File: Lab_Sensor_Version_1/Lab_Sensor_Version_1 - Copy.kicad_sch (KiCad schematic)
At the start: 28 parts, among them U1 ESP32-POE, U2 AM2302, U3 SSD1306, U4 INMP441

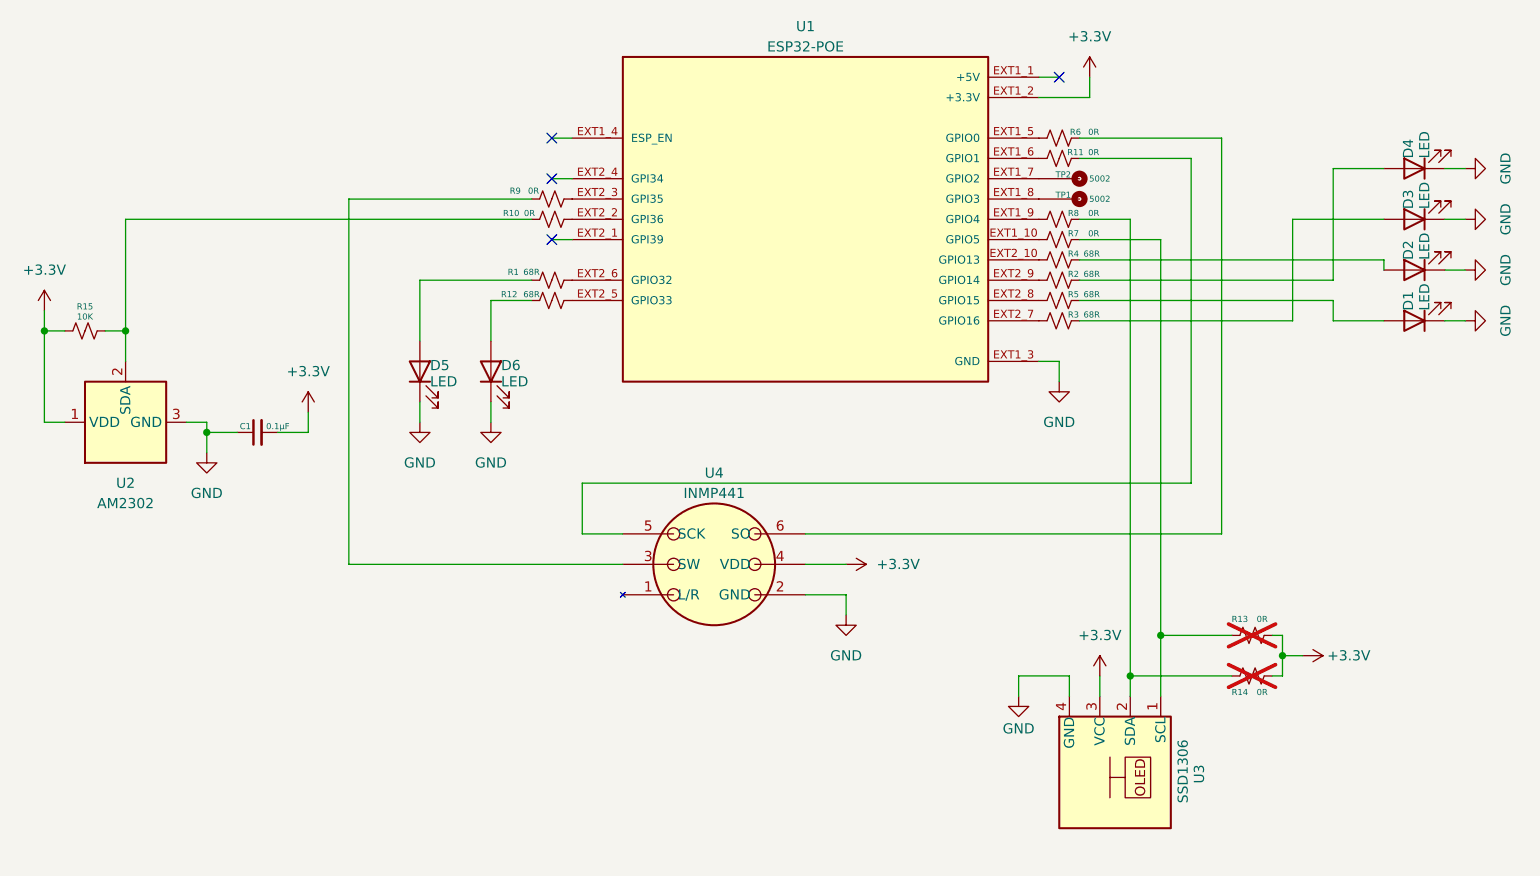
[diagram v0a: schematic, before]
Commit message: Signals on PCB connected
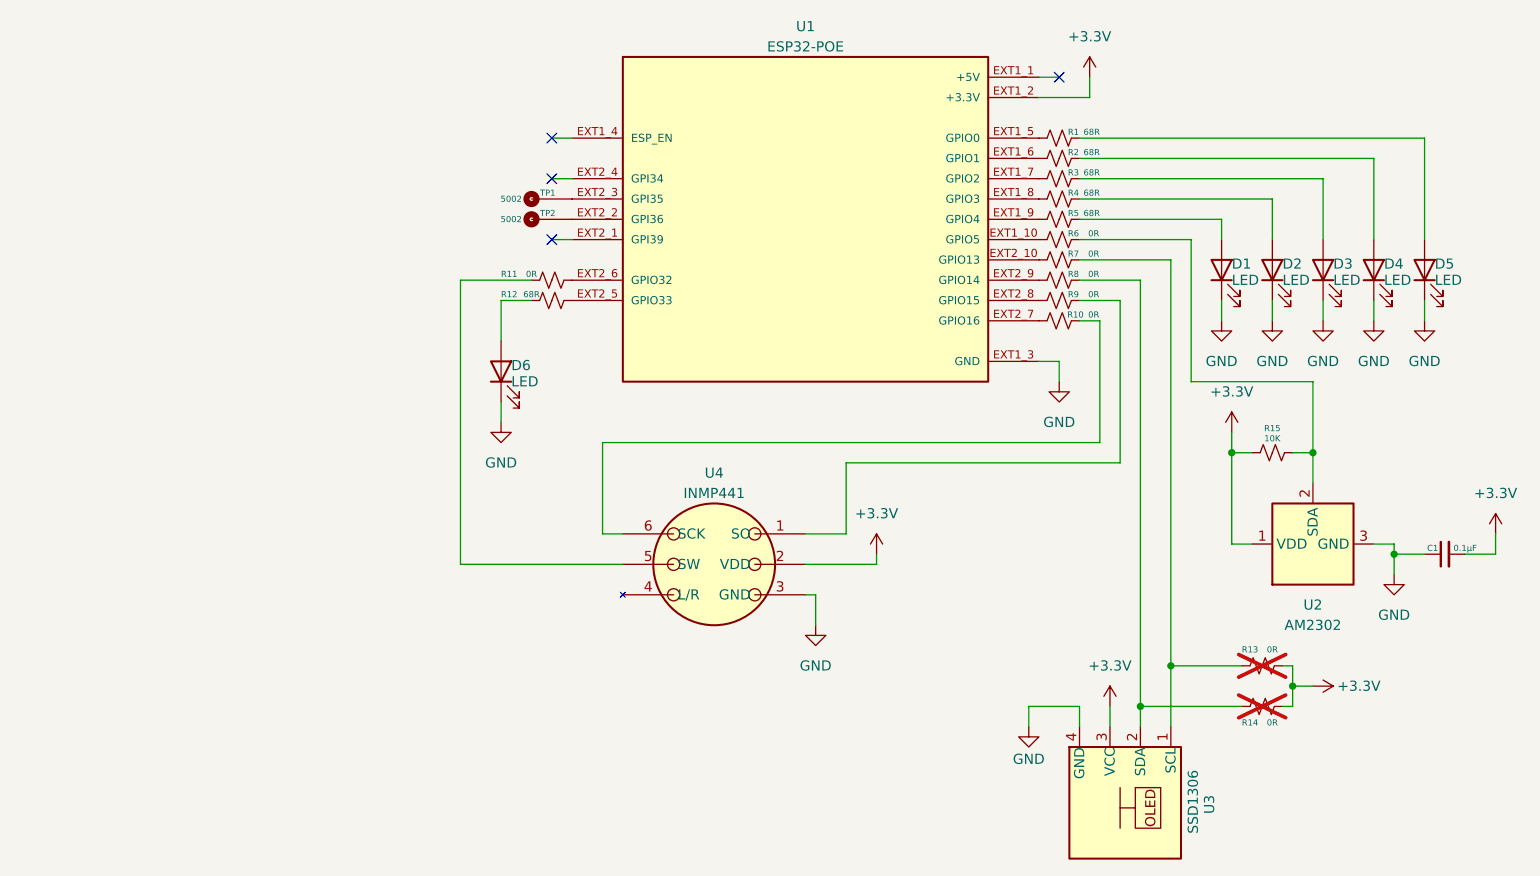
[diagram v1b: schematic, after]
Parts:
- renumbered R6 to R10, R10 to R6
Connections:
- net +3.3V: now also U4.2 (VDD); no longer U4.4 (VDD)
- net GND: now also U4.3 (GND); no longer U4.2 (GND)
- net at R3.2: now also U1.EXT1_7 (GPIO2); no longer U1.EXT2_7 (GPIO16)
- net at R9.1: now also U4.1 (SO); no longer U1.EXT2_3 (GPI35)
- net at R9.2: now also U1.EXT2_8 (GPIO15); no longer U4.3 (SW)
- net at R6.1: now also R15.1, U2.2 (SDA); no longer U1.EXT2_2 (GPI36)
- net at U1.EXT1_10 (GPIO5): now also R6.2; no longer R7.2
- net at TP1.TP: now also U1.EXT2_3 (GPI35); no longer U1.EXT1_8 (GPIO3)
- net at R8.2: now also U1.EXT2_9 (GPIO14); no longer U1.EXT1_9 (GPIO4)
- net at R10.2: now also U1.EXT2_7 (GPIO16); no longer U1.EXT1_5 (GPIO0)
- net at U1.EXT1_6 (GPIO1): now also R2.2; no longer R11.2
- net at TP2.TP: now also U1.EXT2_2 (GPI36); no longer U1.EXT1_7 (GPIO2)
- net at U1.EXT2_10 (GPIO13): now also R7.2; no longer R4.2
- net at U1.EXT2_6 (GPIO32): now also R11.1; no longer R1.1
- net at R5.2: now also U1.EXT1_9 (GPIO4); no longer U1.EXT2_8 (GPIO15)
- net at R1.2: now also U1.EXT1_5 (GPIO0); no longer D5.A
- net at U4.5 (SW): now also R11.2; no longer R11.1
- new net: R4.2, U1.EXT1_8 (GPIO3)
- new net: D5.A, R1.1
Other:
- moved on the sheet: C1, D1, D2, D3, D4, D5, D6, R1, R10, R11, R13, R14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
